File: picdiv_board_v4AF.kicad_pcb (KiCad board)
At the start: 2 copper layers, 75 x 100 mm, 99 parts, among them J1 DC-Input, J10 PPS_B, J101 MountingHole_M2.5, J102 Conn_Coaxial, J103 Conn_Coaxial, J104 MountingHole_M2.5, J105 Conn_01x06, J106 PPS_A, J107 PPS_A, J14 TEST_1PPS, J4 SYNC, J6 PPS_B, J8 SYNC, Q1 Q_PNP_BEC, Q2 Q_PNP_BEC, SW101 SW_DIP_x03, U1 LT1963AxST-3.3, U103 LT1963AEQ, U104 LTC6993xS6-1, U105 IDT5PB1108, U2 LT1963AxST-3.3, U3 PIC12F675, U4 LT1963AEQ, U6 IDT5PB1108, U7 ADR4540, U8 PIC12F675-xMC

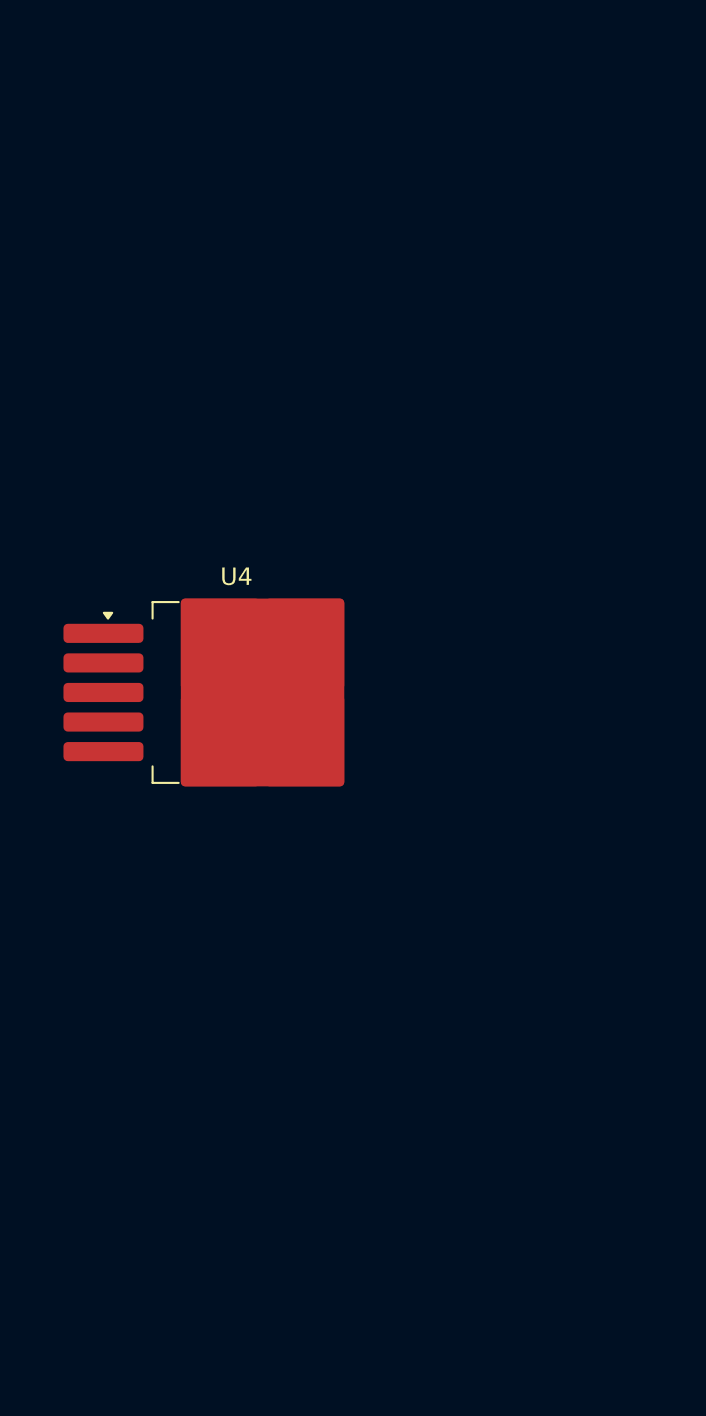
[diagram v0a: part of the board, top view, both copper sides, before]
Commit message: Add missing footprints
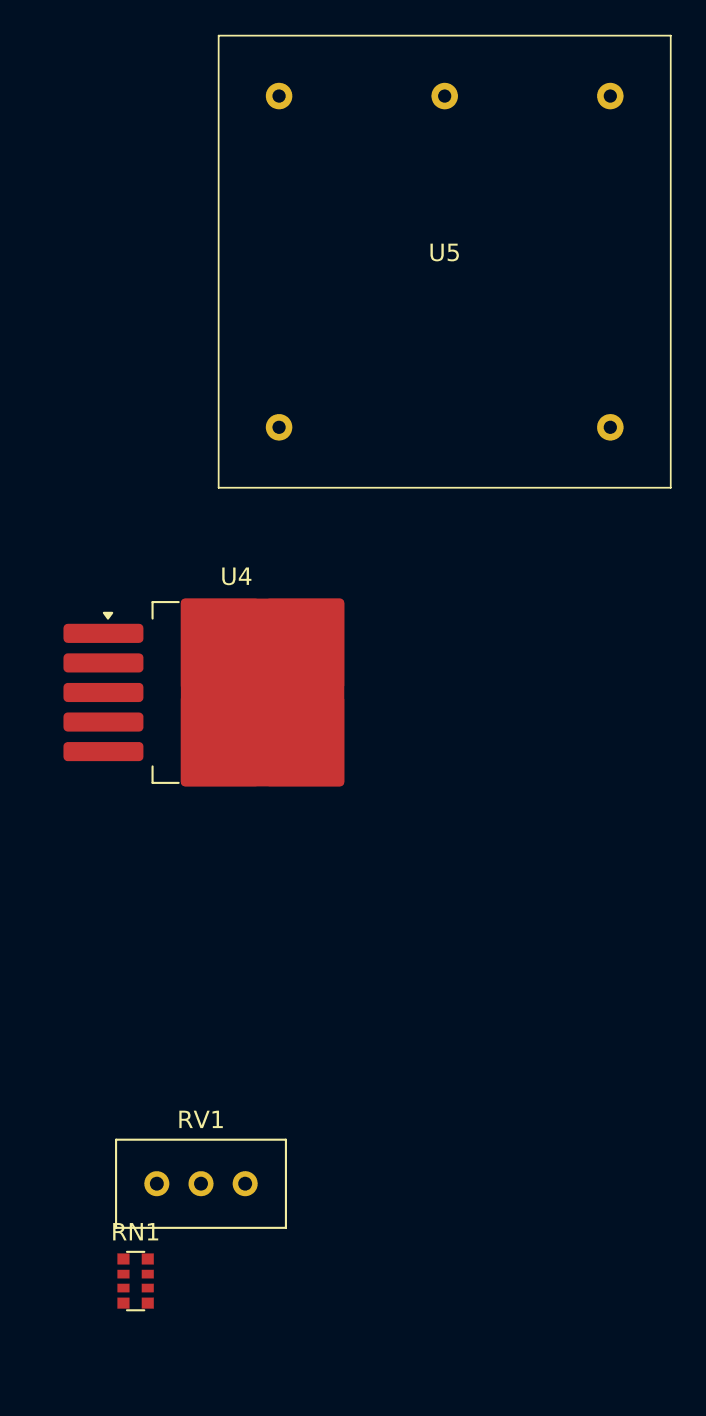
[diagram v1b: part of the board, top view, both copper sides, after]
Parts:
- added RN1: 1K 0.1% ±15ppm, Resistor_SMD:R_Array_Convex_4x0612, F.Cu at (222.2, 115.6)
- added RV1: 2K, Potentiometer_THT:Potentiometer_Bourns_3296W_Vertical, F.Cu at (228.5, 110.0)
- added U5: ~, Oscilator_Local:OSC5A2B02, F.Cu at (240.0, 57.0)

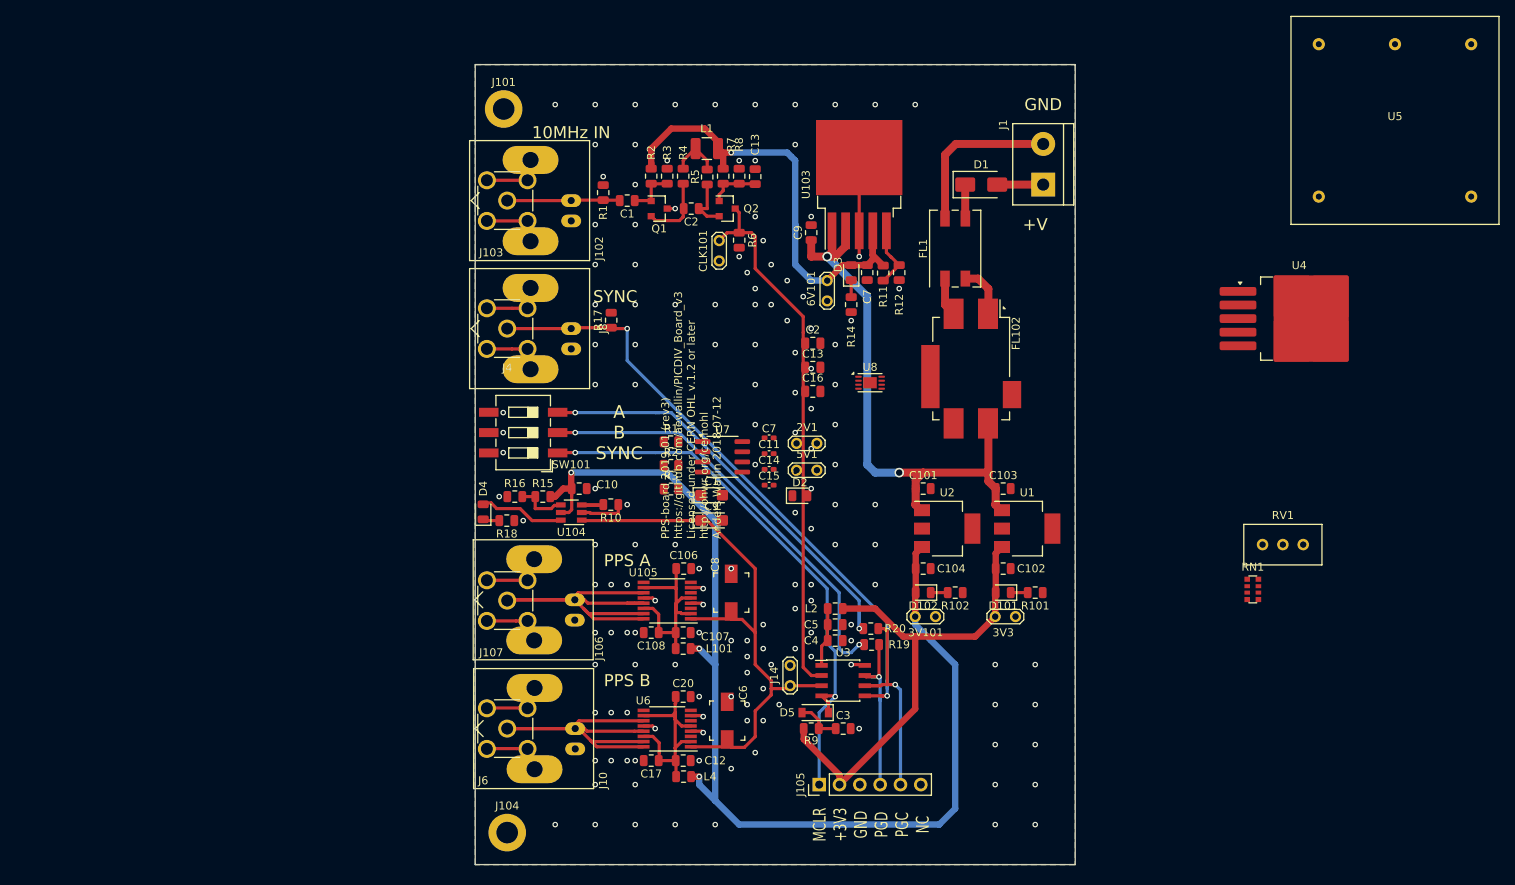
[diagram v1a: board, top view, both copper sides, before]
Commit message: A bit of layout work
Remove sine to square parts from layout.  We don't need it.
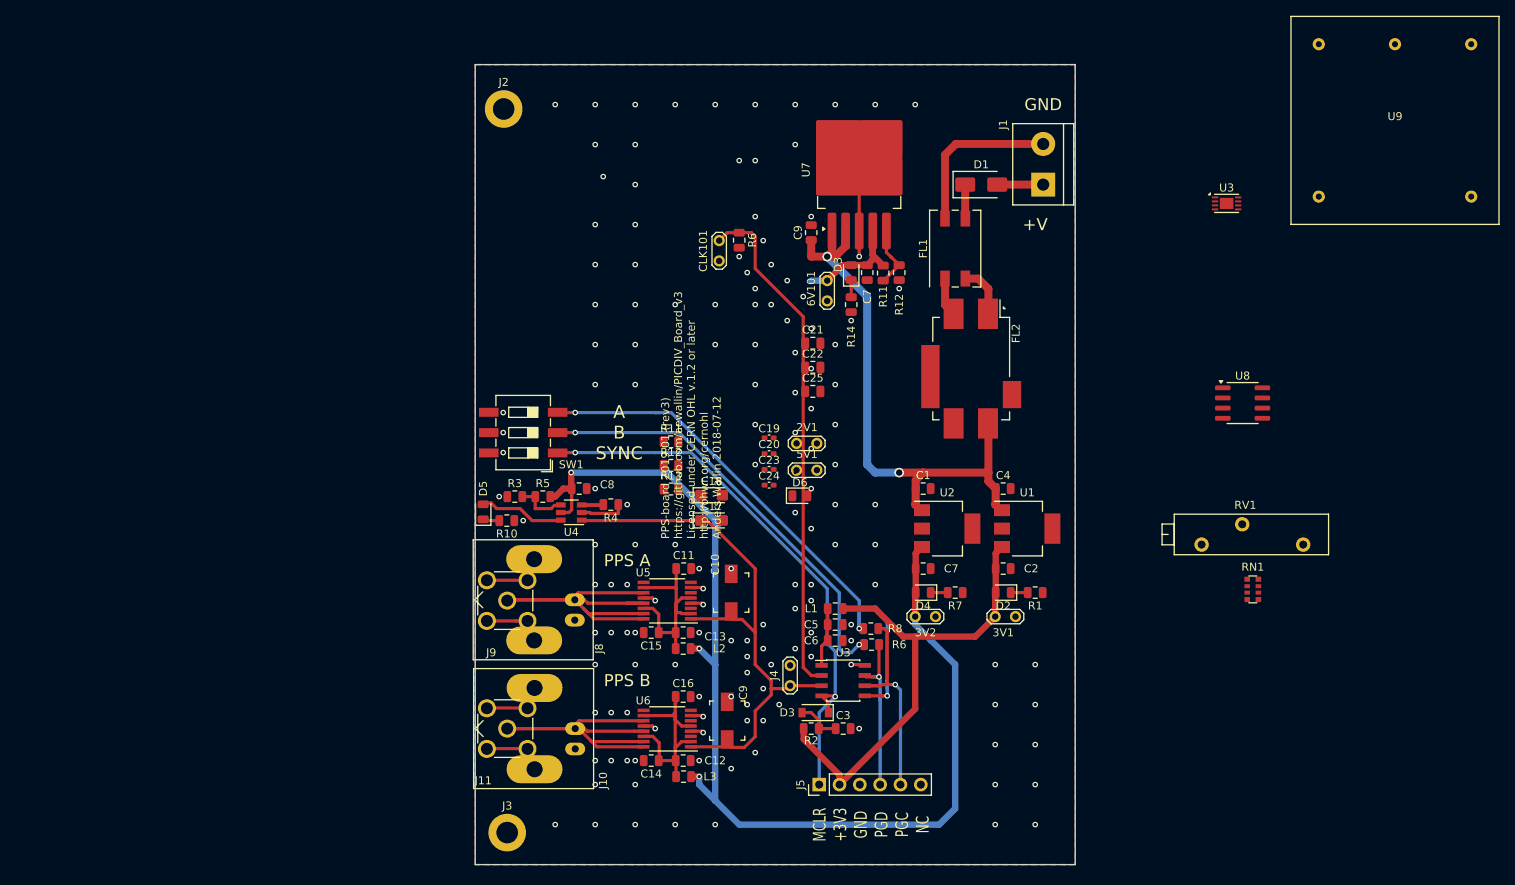
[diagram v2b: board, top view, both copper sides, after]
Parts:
- removed the C1 at (144.0, 67.0)
- removed the C13 at (160.0, 64.0)
- removed the C2 at (152.0, 68.0)
- removed J102: Conn_Coaxial, Connector_Coaxial:BNC_Amphenol_B6252HB-NPP3G-50_Horizontal
- removed J103: Conn_Coaxial, Connector_Coaxial:SMA_Molex_73251-2200_Horizontal
- removed the J4 at (129.0, 83.0)
- removed the J8 at (137.0, 83.0)
- removed the L1 at (153.9, 60.5)
- removed Q1, Q2: Q_PNP_BEC, TO_SOT_Packages_SMD:SOT-23
- removed the R1 at (141.0, 66.0)
- removed R17: 50R, Resistor_SMD:R_0805_2012Metric
- removed the R2 at (147.0, 64.0)
- removed the R3 at (149.0, 64.0)
- removed the R4 at (151.0, 64.0)
- removed the R5 at (154.0, 64.0)
- removed the R7 at (156.0, 64.0)
- removed the R8 at (158.0, 64.0)
- removed U103: LT1963AEQ, Package_TO_SOT_SMD:TO-263-5_TabPin3
- RV1: footprint Potentiometer_THT:Potentiometer_Bourns_3296W_Vertical -> Potentiometer_THT:Potentiometer_Bourns_3006P_Horizontal
- moved U8 65.4 mm to (220.9, 92.3)
- moved U7 58.1 mm to (173.0, 63.1), turned to 90 degrees
- moved U3 49.9 mm to (218.9, 67.3)
- renumbered 3V3 to 3V1, 3V101 to 3V2, C101 to C1, C8 to C10, C106 to C11, C107 to C13, C17 to C14, C108 to C15, C20 to C16, C9 to C17, C1 to C18, C7 to C19, C102 to C2, C11 to C20, C2 to C21, C13 to C22, C14 to C23, C15 to C24, C16 to C25, C103 to C4, C4 to C6, C104 to C7, C10 to C8, C6 to C9, D101 to D2, D5 to D3, D102 to D4, D4 to D5, D2 to D6, FL102 to FL2, J6 to J11, J101 to J2, J104 to J3, J14 to J4, J105 to J5, J106 to J8, J107 to J9, L2 to L1, L101 to L2, L4 to L3, R101 to R1, R18 to R10, R1 to R11, R2 to R12, R3 to R13, R9 to R2, R16 to R3, R10 to R4, R15 to R5, R19 to R6, R102 to R7, R20 to R8, SW101 to SW1, U8 to U3, U104 to U4, U105 to U5, U4 to U7, U7 to U8, U5 to U9
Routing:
- net /sync: track 78.6 -> 13.5 mm, vias 2 -> 1
- net +6V: track 60.8 -> 17.3 mm, vias 1 -> 0
- net GND: track 76.4 -> 55.1 mm, vias 150 -> 148
- net Net-(C1-Pad2): track 14.1 -> 0.00 mm
- net Net-(C2-Pad2): track 8.58 -> 0.00 mm
- net Net-(C2-Pad1): track 6.89 -> 0.00 mm
- net Net-(C13-Pad1): track 6.40 -> 0.00 mm
- net Net-(L1-Pad2): track 6.34 -> 0.00 mm
- net Net-(C1-Pad1): track 6.17 -> 0.00 mm
- net CLK: track 67.4 -> 64.2 mm
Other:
- board text added: "99.5mm wide to fit Hammond 1455"
- board text removed: "100mm vertically into 3U rack-box. for horizontal mounting into 1U box, consider 99mm wide PCB, to mount 4pcs side-by-side at 100mm intervals?"
- board text removed: "10MHz IN"
- board text removed: "10MHz input"
- board text removed: "SYNC"
- board text removed: "SYNC input"

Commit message: More Layout
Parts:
- added R9: 50R, Resistor_SMD:R_0805_2012Metric, F.Cu at (251.3, 137.2)
- U3: value PIC12F675-xMC -> PIC12F675-xSN; footprint Package_DFN_QFN:DFN-8-1EP_3x2mm_P0.5mm_EP1.7x1.4mm -> Package_SO:SOIC-8_3.9x4.9mm_P1.27mm
- moved U3 68.2 mm to (220.5, 135.5)

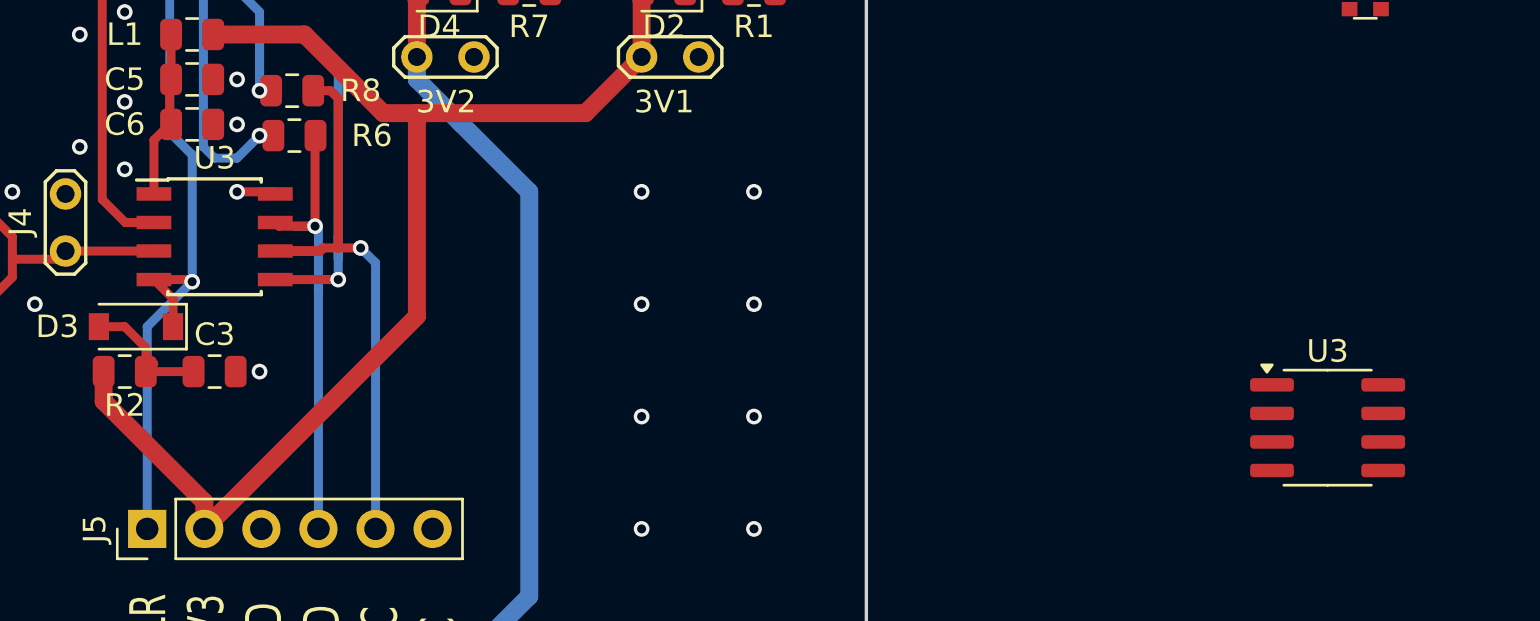
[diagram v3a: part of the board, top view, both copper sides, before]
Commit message: More layout
Appears to be problem with PIC symbol.  I think the library changed on me.
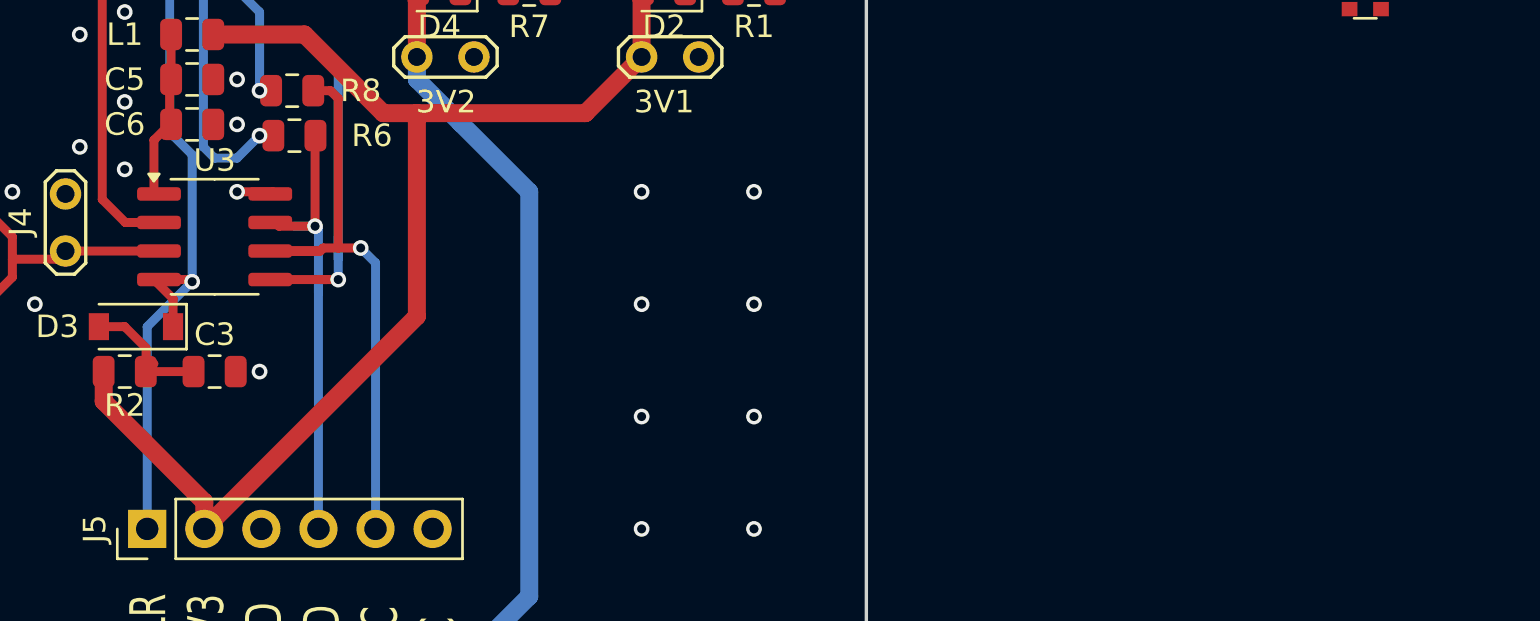
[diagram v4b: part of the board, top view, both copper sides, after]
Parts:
- removed the U3 at (171.0, 127.0)
- moved U3 50.2 mm to (171.0, 127.0)
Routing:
- net 10MHz: track 0.00 -> 13.5 mm, vias 0 -> 1
- net /sync: track 13.5 -> 0.00 mm, vias 1 -> 0
- net Net-(U3-VDD): track 0.00 -> 7.38 mm
- net Net-(C4-Pad1): track 7.38 -> 0.00 mm
